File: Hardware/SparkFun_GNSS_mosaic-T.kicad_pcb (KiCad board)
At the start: 4 copper layers, 50.8 x 50.8 mm, 20 parts, among them J1 Qwiic_RA, U2 RT9080-3.3

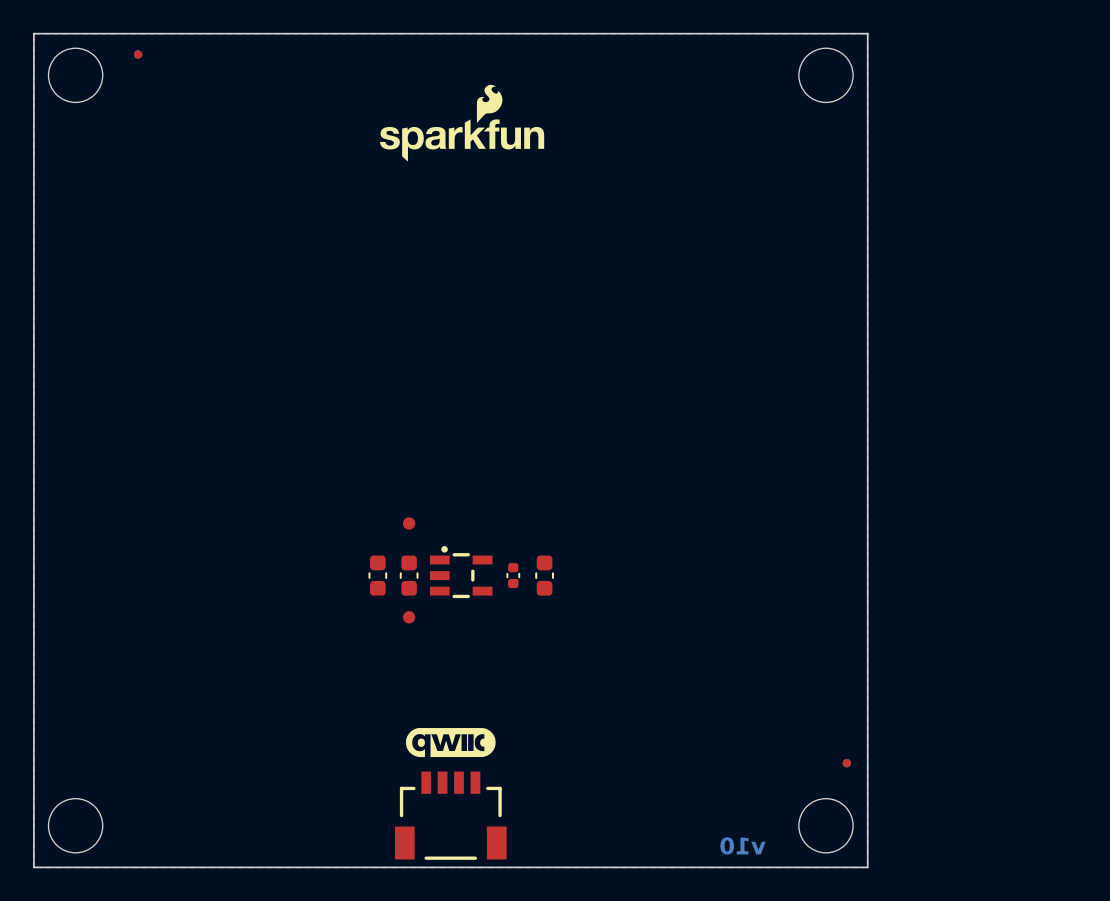
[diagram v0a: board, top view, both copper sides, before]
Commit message: Ready for airwire review
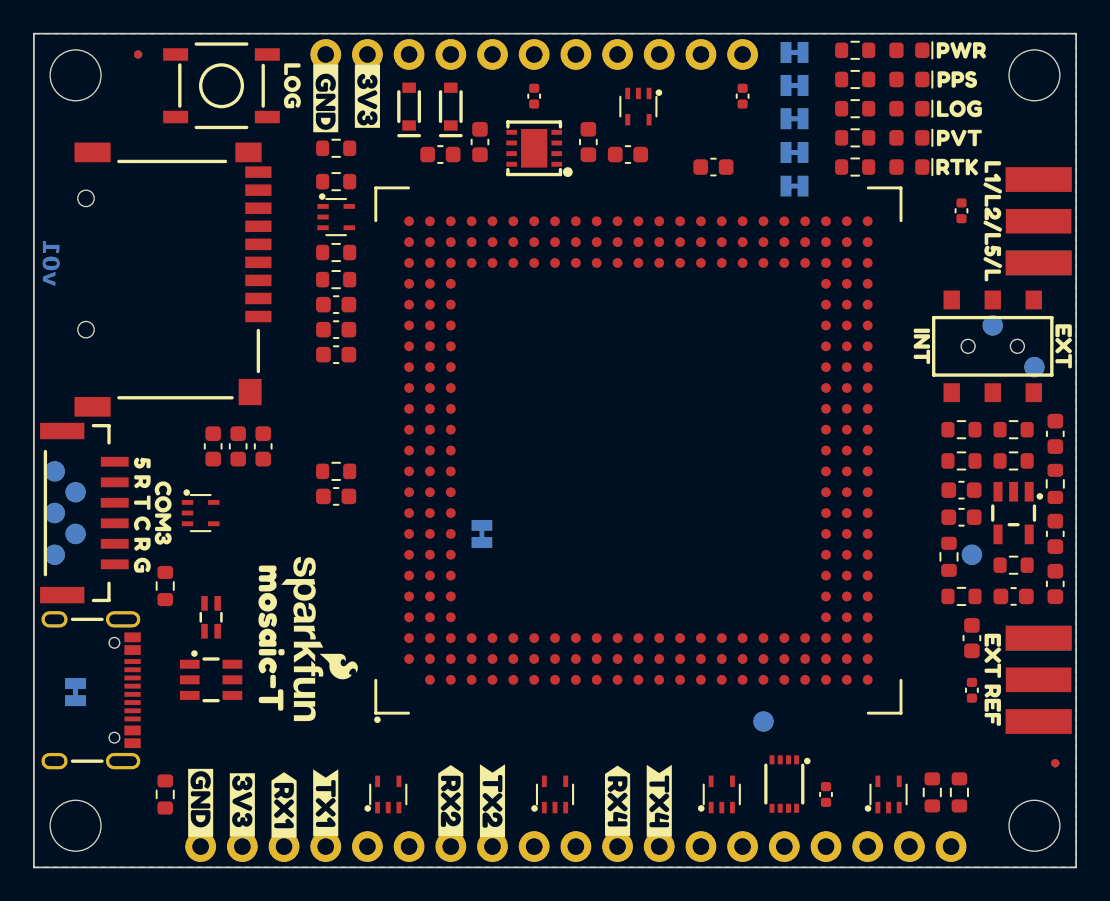
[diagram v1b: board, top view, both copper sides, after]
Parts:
- removed the G*** at (141.0, 116.8)
- removed the G*** at (128.3, 108.0)
- added C1: 10uF, SparkFun-Capacitor:C_0603_1608Metric, F.Cu at (134.0, 90.2)
- added C10: 1.0nF, SparkFun-Capacitor:C_0603_1608Metric, F.Cu at (172.7, 110.5)
- added C11: 1.0nF, SparkFun-Capacitor:C_0603_1608Metric, F.Cu at (175.3, 108.0)
- added C12: 10uF, SparkFun-Capacitor:C_0603_1608Metric, F.Cu at (177.8, 104.1)
- added C13: 0.1uF, SparkFun-Capacitor:C_0603_1608Metric, F.Cu at (177.8, 107.2)
- added C14: 33pF, SparkFun-Capacitor:C_0603_1608Metric, F.Cu at (177.8, 98.0)
- added C15: 10uF, SparkFun-Capacitor:C_0603_1608Metric, F.Cu at (140.3, 81.0)
- added C16: 1.0uF, SparkFun-Capacitor:C_0603_1608Metric, F.Cu at (142.7, 80.3)
- added C17: 1.0uF, SparkFun-Capacitor:C_0603_1608Metric, F.Cu at (151.8, 81.0)
- added C18: 10uF, SparkFun-Capacitor:C_0603_1608Metric, F.Cu at (149.4, 80.3)
- added C6: 0.1uF, SparkFun-Capacitor:C_0603_1608Metric, F.Cu at (172.1, 103.1)
- added C7: 10uF, SparkFun-Capacitor:C_0603_1608Metric, F.Cu at (129.5, 98.8)
- added C8: 0.1uF, SparkFun-Capacitor:C_0603_1608Metric, F.Cu at (126.5, 98.8)
- added C9: 1.0uF, SparkFun-Capacitor:C_0603_1608Metric, F.Cu at (128.0, 98.8)
- added D1: DF5A5.6LFU, SparkFun-Semiconductor-Standard:SOT-353, F.Cu at (134.0, 84.8)
- added D10: DF5A5.6LFU, SparkFun-Semiconductor-Standard:SOT-353, F.Cu at (167.6, 120.0)
- added D11: DF5A5.6LFU, SparkFun-Semiconductor-Standard:SOT-353, F.Cu at (157.5, 120.0)
- added D12: DF5A5.6LFU, SparkFun-Semiconductor-Standard:SOT-353, F.Cu at (147.3, 120.0)
- added D13: DF5A5.6LFU, SparkFun-Semiconductor-Standard:SOT-353, F.Cu at (137.2, 120.0)
- added D14: DF5A5.6LFU, SparkFun-Semiconductor-Standard:SOT-353, F.Cu at (125.7, 102.9)
- added D15: PESD0402, SparkFun-Capacitor:C_0402_1005Metric, F.Cu at (163.8, 120.0)
- added D16: PESD0402, SparkFun-Capacitor:C_0402_1005Metric, F.Cu at (172.7, 113.7)
- added D17: DT1042-04SO, SparkFun-Semiconductor-Standard:SOT23-6, F.Cu at (126.4, 113.0)
- added D18: BAT60A, SparkFun-Semiconductor-Standard:SOD-323, F.Cu at (141.0, 78.1)
- added D19: BAT60A, SparkFun-Semiconductor-Standard:SOD-323, F.Cu at (138.4, 78.1)
- added D2: Red, SparkFun-LED:LED_0603_1608Metric_Red, F.Cu at (168.9, 74.7)
- added D20: PESD0402, SparkFun-Capacitor:C_0402_1005Metric, F.Cu at (158.8, 77.5)
- added D3: Blue, SparkFun-LED:LED_0603_1608Metric_Blue, F.Cu at (168.9, 80.0)
- added D4: Green, SparkFun-LED:LED_0603_1608Metric_Green, F.Cu at (168.9, 78.2)
- added D5: White, SparkFun-LED:LED_0603_1608Metric_White, F.Cu at (168.9, 81.8)
- added D6: Yellow, SparkFun-LED:LED_0603_1608Metric_Yellow, F.Cu at (168.9, 76.5)
- added D7: DF5A5.6LFU, SparkFun-Semiconductor-Standard:SOT-353, F.Cu at (152.4, 78.1)
- added D8: PESD0402, SparkFun-Capacitor:C_0402_1005Metric, F.Cu at (146.1, 77.5)
- added D9: PESD0402, SparkFun-Capacitor:C_0402_1005Metric, F.Cu at (172.1, 84.5)
- added G***: LOGO, SparkFun-Aesthetic:SparkFun_Logo_15mm, B.Cu at (158.8, 99.1)
- added J2: SMA_Edge, SparkFun-Connector:SMA_Edge, F.Cu at (176.8, 85.1)
- added J3: Conn_01x11, SparkFun-Connector:1x11, F.Cu at (133.3, 74.9)
- added J4: Conn_01x19, SparkFun-Connector:1x19, F.Cu at (125.7, 123.2)
- added J5: JST_Locking_6, SparkFun-Connector:JST_SMD_1.25mm-6_Locking, F.Cu at (118.7, 102.9)
- added J6: SMA_Edge, SparkFun-Connector:SMA_Edge, F.Cu at (176.8, 113.0)
- added J7: USB_C_Receptacle, SparkFun-Connector:USB-C_16, F.Cu at (121.9, 113.7)
- added L1: 470Ohm, SparkFun-Capacitor:C_0603_1608Metric, F.Cu at (157.0, 81.8)
- added LOG1: ~, SparkFun-Jumper:Jumper_2_NC_Trace, B.Cu at (161.9, 78.8)
- added PPS1: ~, SparkFun-Jumper:Jumper_2_NC_Trace, B.Cu at (161.9, 76.8)
- added PVT1: ~, SparkFun-Jumper:Jumper_2_NC_Trace, B.Cu at (161.9, 80.9)
- added PWR1: ~, SparkFun-Jumper:Jumper_2_NC_Trace, B.Cu at (161.9, 74.8)
- added R1: 10k, SparkFun-Resistor:R_0603_1608Metric, F.Cu at (134.0, 82.7)
- added R10: 330, SparkFun-Resistor:R_0603_1608Metric, F.Cu at (165.6, 78.2)
- added R11: 1k, SparkFun-Resistor:R_0603_1608Metric, F.Cu at (165.6, 81.8)
- added R12: 2.2k, SparkFun-Resistor:R_0603_1608Metric, F.Cu at (165.6, 76.5)
- added R13: 1k, SparkFun-Resistor:R_0603_1608Metric, F.Cu at (134.0, 80.6)
- added R14: 49.9, SparkFun-Resistor:R_0603_1608Metric, F.Cu at (172.1, 108.0)
- added R15: 1k, SparkFun-Resistor:R_0603_1608Metric, F.Cu at (172.1, 99.7)
- added R16: 1k, SparkFun-Resistor:R_0603_1608Metric, F.Cu at (175.3, 106.0)
- added R17: 5.1k, SparkFun-Resistor:R_0603_1608Metric, F.Cu at (123.6, 120.0)
- added R18: 5.1k, SparkFun-Resistor:R_0603_1608Metric, F.Cu at (123.6, 107.3)
- added R19: 100k, SparkFun-Resistor:R_0603_1608Metric, F.Cu at (175.3, 99.7)
- added R2: 10k, SparkFun-Resistor:R_0603_1608Metric, F.Cu at (134.0, 87.0)
- added R20: 33, SparkFun-Resistor:R_0603_1608Metric, F.Cu at (177.8, 101.1)
- added R21: 1k, SparkFun-Resistor:R_0603_1608Metric, F.Cu at (175.3, 97.8)
- added R22: 1k, SparkFun-Resistor:R_0603_1608Metric, F.Cu at (172.1, 97.8)
- added R3: 10k, SparkFun-Resistor:R_0603_1608Metric, F.Cu at (134.0, 100.3)
- added R4: 10k, SparkFun-Resistor:R_0603_1608Metric, F.Cu at (134.0, 88.6)
- added R5: 10k, SparkFun-Resistor:R_0603_1608Metric, F.Cu at (171.3, 105.5)
- added R6: 4.7k, SparkFun-Resistor:R_0603_1608Metric, F.Cu at (165.6, 74.7)
- added R7: 2.2k, SparkFun-Resistor:R_0603_1608Metric, F.Cu at (165.6, 80.0)
- added R8: 169k, SparkFun-Resistor:R_0603_1608Metric, F.Cu at (170.3, 119.9)
- added R9: 169k, SparkFun-Resistor:R_0603_1608Metric, F.Cu at (172.0, 119.9)
- added RTK1: ~, SparkFun-Jumper:Jumper_2_NC_Trace, B.Cu at (161.9, 82.9)
- added Ref**: Val**, SparkFun-Aesthetic:OSHW_Logo_5mm, B.Cu at (133.3, 99.1)
- added SHLD1: ~, SparkFun-Jumper:Jumper_2_NC_Trace, B.Cu at (118.1, 113.8)
- added SW1: DPDT_Slide_SMD_7.2x3.5mm, SparkFun-Switch:Slide_DPDT_SMD_7.2x3.5mm, F.Cu at (174.0, 92.7)
- added SW2: SMD_5.2x5.2mm_h2.5mm, SparkFun-Switch:Push_SMD_5.2x5.2mm_h2.5mm, F.Cu at (127.0, 76.8)
- added TP10: 1.25mm, SparkFun-Connector:TestPoint-1.25mm, B.Cu at (176.5, 94.0)
- added TP11: 1.25mm, SparkFun-Connector:TestPoint-1.25mm, B.Cu at (116.8, 100.3)
- added TP3: 1.25mm, SparkFun-Connector:TestPoint-1.25mm, B.Cu at (160.0, 115.6)
- added TP4: 1.25mm, SparkFun-Connector:TestPoint-1.25mm, B.Cu at (116.8, 105.4)
- added TP5: 1.25mm, SparkFun-Connector:TestPoint-1.25mm, B.Cu at (118.1, 104.1)
- added TP6: 1.25mm, SparkFun-Connector:TestPoint-1.25mm, B.Cu at (116.8, 102.9)
- added TP7: 1.25mm, SparkFun-Connector:TestPoint-1.25mm, B.Cu at (118.1, 101.6)
- added TP8: 1.25mm, SparkFun-Connector:TestPoint-1.25mm, B.Cu at (176.8, 113.0)
- added TR1: RFCMF1220100M4T, SparkFun-Coil:RFCMF1220100M4T, F.Cu at (126.4, 109.2)
- added U1: mosaic-T, SparkFun-GPS:MOSAIC_LGA, F.Cu at (152.4, 99.1)
- added U3: LMV7219M5, SparkFun-Semiconductor-Standard:SOT23-5, F.Cu at (175.3, 102.9)
- added U4: AP7361C-3.3V, SparkFun-Semiconductor-Standard:UDFN-8, F.Cu at (146.1, 80.6)
- added VBATT1: ~, SparkFun-Jumper:Jumper_2_NC_Trace, B.Cu at (142.9, 104.1)
- added kibuzzard-67D02274: G***, kibuzzard-67D02274, F.Cu at (172.1, 74.7)
- added kibuzzard-67D02289: G***, kibuzzard-67D02289, F.Cu at (171.8, 76.5)
- added kibuzzard-67D02298: G***, kibuzzard-67D02298, F.Cu at (172.0, 78.2)
- added kibuzzard-67D02298: G***, kibuzzard-67D02298, F.Cu at (131.3, 76.8)
- added kibuzzard-67D022A2: G***, kibuzzard-67D022A2, F.Cu at (172.0, 80.0)
- added kibuzzard-67D022AC: G***, kibuzzard-67D022AC, F.Cu at (171.8, 81.8)
- added kibuzzard-67D0352E: G***, kibuzzard-67D0352E, F.Cu at (130.0, 110.5)
- added kibuzzard-67D03557: G***, kibuzzard-67D03557, B.Cu at (154.9, 99.1)
- added kibuzzard-67D0356E: G***, kibuzzard-67D0356E, B.Cu at (151.1, 99.1)
- added kibuzzard-67D03584: G***, kibuzzard-67D03584, B.Cu at (147.3, 99.1)
- added kibuzzard-67D035E7: G***, kibuzzard-67D035E7, F.Cu at (169.7, 92.7)
- added kibuzzard-67D035FF: G***, kibuzzard-67D035FF, F.Cu at (178.3, 92.7)
- added kibuzzard-67D03C98: G***, kibuzzard-67D03C98, F.Cu at (174.0, 85.1)
- added kibuzzard-67D03CC5: G***, kibuzzard-67D03CC5, F.Cu at (174.0, 113.0)
- added kibuzzard-67D044A8: G***, kibuzzard-67D044A8, F.Cu at (133.3, 77.6)
- added kibuzzard-67D044BC: G***, kibuzzard-67D044BC, F.Cu at (135.9, 77.5)
- added kibuzzard-67D044ED: G***, kibuzzard-67D044ED, F.Cu at (125.7, 120.5)
- added kibuzzard-67D04501: G***, kibuzzard-67D04501, F.Cu at (128.3, 120.7)
- added kibuzzard-67D0451A: G***, kibuzzard-67D0451A, F.Cu at (130.8, 120.7)
- added kibuzzard-67D04530: G***, kibuzzard-67D04530, F.Cu at (133.3, 120.5)
- added kibuzzard-67D0454D: G***, kibuzzard-67D0454D, F.Cu at (141.0, 120.4)
- added kibuzzard-67D0455C: G***, kibuzzard-67D0455C, F.Cu at (143.5, 120.4)
- added kibuzzard-67D04570: G***, kibuzzard-67D04570, F.Cu at (151.1, 120.4)
- added kibuzzard-67D04579: G***, kibuzzard-67D04579, F.Cu at (153.7, 120.4)
- added kibuzzard-67D045AD: G***, kibuzzard-67D045AD, B.Cu at (125.7, 120.5)
- added kibuzzard-67D045C9: G***, kibuzzard-67D045C9, B.Cu at (128.3, 120.7)
- added kibuzzard-67D045EC: G***, kibuzzard-67D045EC, B.Cu at (130.8, 120.7)
- added kibuzzard-67D04612: G***, kibuzzard-67D04612, B.Cu at (133.3, 120.5)
- added kibuzzard-67D04639: G***, kibuzzard-67D04639, B.Cu at (135.9, 120.1)
- added kibuzzard-67D04669: G***, kibuzzard-67D04669, B.Cu at (138.4, 120.1)
- added kibuzzard-67D046A8: G***, kibuzzard-67D046A8, B.Cu at (141.0, 120.4)
- added kibuzzard-67D046B5: G***, kibuzzard-67D046B5, B.Cu at (143.5, 120.3)
- added kibuzzard-67D046BD: G***, kibuzzard-67D046BD, B.Cu at (146.1, 120.0)
- added kibuzzard-67D046CC: G***, kibuzzard-67D046CC, B.Cu at (148.6, 119.9)
- added kibuzzard-67D046F7: G***, kibuzzard-67D046F7, B.Cu at (151.1, 120.4)
- added kibuzzard-67D046FF: G***, kibuzzard-67D046FF, B.Cu at (153.7, 120.4)
- added kibuzzard-67D04726: G***, kibuzzard-67D04726, B.Cu at (156.2, 120.5)
- added kibuzzard-67D0474E: G***, kibuzzard-67D0474E, B.Cu at (158.8, 120.4)
- added kibuzzard-67D04771: G***, kibuzzard-67D04771, B.Cu at (161.3, 120.4)
- added kibuzzard-67D047AD: G***, kibuzzard-67D047AD, B.Cu at (163.8, 118.5)
- added kibuzzard-67D047C3: G***, kibuzzard-67D047C3, B.Cu at (166.4, 120.5)
- added kibuzzard-67D047D9: G***, kibuzzard-67D047D9, B.Cu at (168.9, 118.4)
- added kibuzzard-67D047EC: G***, kibuzzard-67D047EC, B.Cu at (171.4, 118.5)
- added kibuzzard-67D04943: G***, kibuzzard-67D04943, F.Cu at (123.4, 102.9)
- added kibuzzard-67D0498C: G***, kibuzzard-67D0498C, F.Cu at (122.2, 99.8)
- added kibuzzard-67D0498C: G***, kibuzzard-67D0498C, B.Cu at (119.5, 100.3)
- added kibuzzard-67D04998: G***, kibuzzard-67D04998, F.Cu at (122.2, 104.8)
- added kibuzzard-67D04998: G***, kibuzzard-67D04998, F.Cu at (122.2, 101.0)
- added kibuzzard-67D04998: G***, kibuzzard-67D04998, B.Cu at (119.5, 101.6)
- added kibuzzard-67D04998: G***, kibuzzard-67D04998, B.Cu at (119.5, 105.4)
- added kibuzzard-67D049A2: G***, kibuzzard-67D049A2, F.Cu at (122.2, 102.2)
- added kibuzzard-67D049A2: G***, kibuzzard-67D049A2, B.Cu at (119.5, 102.9)
- added kibuzzard-67D049B0: G***, kibuzzard-67D049B0, F.Cu at (122.2, 103.5)
- added kibuzzard-67D049B0: G***, kibuzzard-67D049B0, B.Cu at (119.5, 104.1)
- added kibuzzard-67D049C9: G***, kibuzzard-67D049C9, F.Cu at (122.2, 106.0)
- added kibuzzard-67D04A61: G***, kibuzzard-67D04A61, B.Cu at (165.5, 74.8)
- added kibuzzard-67D04A72: G***, kibuzzard-67D04A72, B.Cu at (165.1, 76.8)
- added kibuzzard-67D04A80: G***, kibuzzard-67D04A80, B.Cu at (165.4, 78.9)
- added kibuzzard-67D04A91: G***, kibuzzard-67D04A91, B.Cu at (165.4, 80.9)
- added kibuzzard-67D04AA3: G***, kibuzzard-67D04AA3, B.Cu at (165.2, 82.9)
- added kibuzzard-67D04B0C: G***, kibuzzard-67D04B0C, B.Cu at (174.0, 89.3)
- added kibuzzard-67D04B28: G***, kibuzzard-67D04B28, B.Cu at (176.5, 97.5)
- added kibuzzard-67D04B58: G***, kibuzzard-67D04B58, B.Cu at (172.7, 103.4)
- added kibuzzard-67D04B80: G***, kibuzzard-67D04B80, B.Cu at (160.0, 113.4)
- added kibuzzard-67D04D07: G***, kibuzzard-67D04D07, B.Cu at (135.9, 77.5)
- added kibuzzard-67D04D20: G***, kibuzzard-67D04D20, B.Cu at (133.3, 77.6)
- added kibuzzard-67D04D30: G***, kibuzzard-67D04D30, B.Cu at (138.4, 77.5)
- added kibuzzard-67D04D50: G***, kibuzzard-67D04D50, B.Cu at (141.0, 78.2)
- added kibuzzard-67D04D99: G***, kibuzzard-67D04D99, B.Cu at (143.5, 78.9)
- added kibuzzard-67D04E18: G***, kibuzzard-67D04E18, B.Cu at (148.6, 77.7)
- added kibuzzard-67D04E6C: G***, kibuzzard-67D04E6C, B.Cu at (146.1, 78.2)
- added kibuzzard-67D04E88: G***, kibuzzard-67D04E88, B.Cu at (151.1, 77.7)
- added kibuzzard-67D04E93: G***, kibuzzard-67D04E93, B.Cu at (153.7, 77.7)
- added kibuzzard-67D04EAA: G***, kibuzzard-67D04EAA, B.Cu at (156.2, 78.0)
- added kibuzzard-67D04FB5: G***, kibuzzard-67D04FB5, B.Cu at (158.8, 79.1)
- added kibuzzard-67D05112: G***, kibuzzard-67D05112, B.Cu at (119.8, 113.8)
- added kibuzzard-67D05125: G***, kibuzzard-67D05125, B.Cu at (141.2, 104.1)
- C3: value 1.0uF -> 0.1uF
- C4: value 1.0uF -> 0.1uF; footprint SparkFun-Capacitor:C_0402_1005Metric -> SparkFun-Capacitor:C_0603_1608Metric
- C5: value 10uF -> 1.0uF
- J1: value Qwiic_RA -> microSD; footprint SparkFun-Connector:JST_SMD_1.0mm-4_Black -> SparkFun-Connector:microSD_External_Pin
- ST1, ST2, ST3, ST4: value Stand_off -> Standoff
- TP1, TP2: value TestPoint_0.75mm -> 1.25mm; footprint SparkFun-Connector:TestPoint-0.75mm -> SparkFun-Connector:TestPoint-1.25mm; moved to B.Cu
- U2: value RT9080-3.3 -> 74LVC2T45DC; footprint SparkFun-Semiconductor-Standard:SOT23-5 -> SparkFun-Semiconductor-Standard:VSSOP8_SOT765-1
- moved J1 37.9 mm to (118.7, 88.6), turned to -90 degrees
- moved TP2 37.6 mm to (174.0, 91.4), turned to 180 degrees
- moved C2 35.9 mm to (172.1, 101.5), turned to 0 degrees
- moved TP1 34.5 mm to (172.7, 105.4), turned to 180 degrees
- moved G*** 31.9 mm to (132.1, 110.5), turned to -90 degrees
- moved U2 23.4 mm to (161.3, 119.4), turned to -90 degrees
- moved C5 19.6 mm to (134.0, 91.7), turned to 180 degrees
- moved C4 17.3 mm to (134.0, 93.2), turned to 180 degrees
- moved FID2 12.7 mm to (177.8, 118.1)
- moved FID4 12.7 mm to (177.8, 118.1)
- moved ST3 12.7 mm to (176.5, 76.2)
- moved ST4 12.7 mm to (176.5, 121.9)
- moved C3 6.56 mm to (134.0, 101.9), turned to 180 degrees
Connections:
- C2 pad 1: VCC -> 1.8V
- C3 pad 1: VCC -> ~{RESET}
- J1 pad 1: GND -> unconnected-(J1-DAT2-Pad1)
- J1 pad 2: 3.3V -> Net-(J1-DAT3/CD)
- J1 pad 3: SDA -> SD_CMD
- J1 pad 4: SCL -> 3.3V
- TP1 pad 1: GND -> 1.8V
- TP2 pad 1: VCC -> 2V8_IN
- U2 pad 1: VCC -> 1.8V
- U2 pad 2: GND -> PPS_1V8
- U2 pad 3: VCC -> PPS_1V8
- U2 pad 4: unconnected-(U2-NC-Pad4) -> GND
- U2 pad 5: 3.3V -> 1.8V
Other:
- board size 50.8 x 50.8 mm -> 63.5 x 50.8 mm
- board text added: "v01"
- board text removed: "v10"

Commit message: Routing - WIP
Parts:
- removed D20: PESD0402, SparkFun-Capacitor:C_0402_1005Metric
- added TP12: 1.25mm, SparkFun-Connector:TestPoint-1.25mm, B.Cu at (128.3, 112.4)
- added TP9: 1.25mm, SparkFun-Connector:TestPoint-1.25mm, B.Cu at (128.3, 114.9)
- added kibuzzard-67D03C98: G***, kibuzzard-67D03C98, B.Cu at (173.4, 85.1)
- added kibuzzard-67D03CC5: G***, kibuzzard-67D03CC5, B.Cu at (173.4, 113.0)
- added kibuzzard-67D16721: G***, kibuzzard-67D16721, B.Cu at (134.6, 116.8)
- added kibuzzard-67D1674C: G***, kibuzzard-67D1674C, B.Cu at (144.8, 116.8)
- added kibuzzard-67D16775: G***, kibuzzard-67D16775, B.Cu at (152.4, 116.8)
- added kibuzzard-67D171AB: G***, kibuzzard-67D171AB, B.Cu at (127.0, 112.4)
- added kibuzzard-67D171E5: G***, kibuzzard-67D171E5, B.Cu at (127.0, 114.9)
- D15, D8: value PESD0402 -> DF5A5.6LFU; footprint SparkFun-Capacitor:C_0402_1005Metric -> SparkFun-Semiconductor-Standard:SOT-353
- moved D8 11.4 mm to (157.5, 77.7)
- moved TR1 6.75 mm to (131.4, 113.7), turned to 0 degrees
- moved kibuzzard-67D04B80 6.56 mm to (166.4, 111.8)
- moved TP3 6.48 mm to (166.4, 114.3)
- moved D15 6.35 mm to (170.2, 120.0), turned to 90 degrees
- moved U2 5.72 mm to (167.0, 119.4)
- moved kibuzzard-67D04B0C 4.44 mm to (174.0, 93.7)
- moved G*** 3.86 mm to (131.4, 106.7)
- moved D10 3.81 mm to (163.8, 120.0)
- moved kibuzzard-67D0352E 3.60 mm to (129.5, 106.9)
- moved R8 3.14 mm to (169.5, 116.8)
- moved R9 3.09 mm to (171.4, 116.8)
- moved L1 2.84 mm to (154.2, 81.3), turned to 0 degrees
- moved D7 2.57 mm to (149.9, 77.7), turned to 90 degrees
- moved R13 1.27 mm to (132.7, 80.6)
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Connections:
- D1 pad 1: SD_CMD -> SD_CLK
- D1 pad 3: SD_CLK -> 3.3V
- D1 pad 4: SD_DATA -> SD_CMD
- D1 pad 5: 3.3V -> SD_DATA
- D10 pad 1: RTK_LED -> LOG_BTN
- D10 pad 4: EVENT_A -> unconnected-(D10-K3-Pad4)
- D10 pad 5: EVENT_B -> RTK_LED
- D11 pad 1: RX4 -> TX4
- D11 pad 3: TX4 -> GP1
- D11 pad 4: GP1 -> GP2
- D11 pad 5: GP2 -> RX4
- D12 pad 1: RX2 -> TX2
- D12 pad 3: TX2 -> RTS2
- D12 pad 4: RTS2 -> CTS2
- D12 pad 5: CTS2 -> RX2
- D13 pad 1: RX1 -> TX1
- D13 pad 3: TX1 -> RTS1
- D13 pad 4: RTS1 -> CTS1
- D13 pad 5: CTS1 -> RX1
- D14 pad 1: RTS3 -> TX3
- D14 pad 4: TX3 -> RTS3
- D15 pad 1: GND -> EVENT_A
- D15 pad 2: LOG_BTN -> GND
- D17 pad 4: unconnected-(D17-I/O3-Pad4) -> Net-(D17-I/O2)
- D17 pad 6: unconnected-(D17-I/O4-Pad6) -> Net-(D17-I/O1)
- D7 pad 1: RDY -> ~{RESET}
- D7 pad 3: PVT_LED -> LOG_LED
- D7 pad 4: LOG_LED -> PVT_LED
- D7 pad 5: PMIC_ON_REQ -> RDY
- D8 pad 1: GND -> PMIC_ON_REQ
- D8 pad 2: ~{RESET} -> GND
- J7 pad A6: Net-(D17-I/O1) -> Net-(D17-I/O2)
- J7 pad A7: Net-(D17-I/O2) -> Net-(D17-I/O1)
- J7 pad B6: Net-(D17-I/O1) -> Net-(D17-I/O2)
- J7 pad B7: Net-(D17-I/O2) -> Net-(D17-I/O1)
- TR1 pad 1: Net-(D17-I/O2) -> Net-(D17-I/O1)
- TR1 pad 3: Net-(D17-I/O1) -> Net-(D17-I/O2)
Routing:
- net 3.3V: track 0.00 -> 214.9 mm, vias 0 -> 5
- net VUSB: track 0.00 -> 90.1 mm, vias 0 -> 4
- net VBATT: track 0.00 -> 73.1 mm, vias 0 -> 2
- net SD_DATA: track 0.00 -> 63.5 mm, vias 0 -> 2
- net SD_CMD: track 0.00 -> 60.6 mm, vias 0 -> 2
- net SD_CLK: track 0.00 -> 60.1 mm, vias 0 -> 2
- net 5V: track 0.00 -> 55.5 mm, vias 0 -> 5
- net TX3: track 0.00 -> 50.9 mm, vias 0 -> 2
- net CTS3: track 0.00 -> 44.9 mm, vias 0 -> 3
- net RTS3: track 0.00 -> 44.1 mm, vias 0 -> 3
- net RX3: track 0.00 -> 42.8 mm, vias 0 -> 3
- net 2V8_IN: track 0.00 -> 29.9 mm, vias 0 -> 2
- net GND: track 0.00 -> 29.2 mm, vias 0 -> 155
- net 2V8_OUT: track 0.00 -> 26.9 mm, vias 0 -> 2
- net TX1: track 0.00 -> 19.0 mm, vias 0 -> 1
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
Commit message: Routed
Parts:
- moved kibuzzard-67D04B80 0.38 mm to (166.4, 112.1)
- turned kibuzzard-67D171AB to 90 degrees
- turned kibuzzard-67D171E5 to 90 degrees
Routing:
- net LOG_BTN: track 2.64 -> 68.8 mm, vias 0 -> 4
- net PPS: track 5.86 -> 67.9 mm, vias 0 -> 2
- net LOG_LED: track 6.06 -> 63.4 mm, vias 0 -> 1
- net RTK_LED: track 5.25 -> 61.8 mm, vias 0 -> 3
- net ON_OFF: track 4.09 -> 48.3 mm, vias 0 -> 2
- net PVT_LED: track 2.49 -> 45.3 mm, vias 0 -> 3
- net ~{RESET}: track 11.4 -> 48.2 mm, vias 0 -> 2
- net RDY: track 2.49 -> 39.3 mm, vias 0 -> 2
- net PMIC_ON_REQ: track 4.09 -> 36.3 mm, vias 0 -> 2
- net TX4: track 4.14 -> 27.2 mm, vias 0 -> 2
- net RX4: track 7.35 -> 28.4 mm, vias 0 -> 2
- net GP2: track 4.42 -> 24.2 mm, vias 0 -> 2
- net GP1: track 3.17 -> 22.2 mm, vias 0 -> 1
- net 1.8V: track 17.5 -> 36.5 mm, vias 1 -> 2
- net PPS_1V8: track 0.00 -> 16.8 mm, vias 0 -> 2
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
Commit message: More updates, post proto review
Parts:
- removed kibuzzard-67D0498C (x2): G***, kibuzzard-67D0498C
- removed kibuzzard-67D049C9: G***, kibuzzard-67D049C9
- added TP13: 1.25mm, SparkFun-Connector:TestPoint-1.25mm, B.Cu at (116.8, 100.3)
- added VOUT1: ~, SparkFun-Jumper:Jumper_3_NC-1_Trace, B.Cu at (124.5, 98.8)
- added kibuzzard-67DABC71: G***, kibuzzard-67DABC71, F.Cu at (122.2, 99.8)
- added kibuzzard-67DABC7B: G***, kibuzzard-67DABC7B, B.Cu at (119.5, 100.3)
- added kibuzzard-67DABC87: G***, kibuzzard-67DABC87, F.Cu at (122.2, 106.0)
- added kibuzzard-67DABED8: G***, kibuzzard-67DABED8, B.Cu at (137.2, 82.9)
- added kibuzzard-67DAC0B5: G***, kibuzzard-67DAC0B5, B.Cu at (122.8, 98.8)
- added kibuzzard-67DAC0E0: G***, kibuzzard-67DAC0E0, B.Cu at (124.5, 101.9)
- added kibuzzard-67DAC106: G***, kibuzzard-67DAC106, B.Cu at (124.5, 95.2)
- moved TP11 27.9 mm to (137.2, 81.3)
- moved kibuzzard-67D04B58 2.36 mm to (171.3, 105.3)
- moved G*** 0.25 mm to (158.8, 99.3)
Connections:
- D10 pad 4: unconnected-(D10-K3-Pad4) -> PPS
- J5 pad 1: 5V -> Net-(J5-Pin_1)
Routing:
- net Net-(J5-Pin_1): track 0.00 -> 10.5 mm, vias 0 -> 2
- net GND: track 29.2 -> 38.6 mm, vias 188 -> 187
- net 3.3V: track 228.0 -> 233.0 mm, vias 6 -> 8
- net CTS3: track 44.9 -> 46.1 mm
- net CTS1: track 12.9 -> 14.0 mm
- net 5V: track 55.5 -> 54.8 mm, vias 5 -> 4
